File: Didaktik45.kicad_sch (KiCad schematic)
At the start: 110 parts, among them J1 Conn_01x04_MountingPin, SW1 SW_Push, SW10 SW_Push_45deg, SW11 SW_Push_45deg, SW12 SW_Push_45deg, SW13 SW_Push_45deg, SW14 SW_Push_45deg, SW15 SW_Push_45deg, SW16 SW_Push_45deg, SW17 SW_Push_45deg, SW18 SW_Push_45deg, SW19 SW_Push_45deg, SW2 SW_Push_45deg, SW20 SW_Push_45deg, SW21 SW_Push_45deg, SW22 SW_Push_45deg, SW23 SW_Push_45deg, SW24 SW_Push_45deg, SW25 SW_Push_45deg, SW26 SW_Push_45deg, SW27 SW_Push_45deg, SW28 SW_Push_45deg, SW29 SW_Push_45deg, SW3 SW_Push_45deg, SW30 SW_Push_45deg, SW31 SW_Push_45deg, SW32 SW_Push_45deg, SW33 SW_Push_45deg, SW34 SW_Push_45deg, SW35 SW_Push_45deg, SW36 SW_Push_45deg, SW37 SW_Push_45deg, SW38 SW_Push_45deg, SW39 SW_Push_45deg, SW4 SW_Push_45deg, SW40 SW_Push_45deg, SW41 SW_Push_45deg, SW42 SW_Push_45deg, SW43 SW_Push_45deg, SW44 SW_Push_45deg, SW45 SW_Push_45deg, SW46 SW_Push_45deg, SW5 SW_Push_45deg, SW6 SW_Push_45deg, SW7 SW_Push_45deg, SW8 SW_Push_45deg, SW9 SW_Push_45deg, U1 ATmega32U4-M, Y1 Crystal_GND24_Small

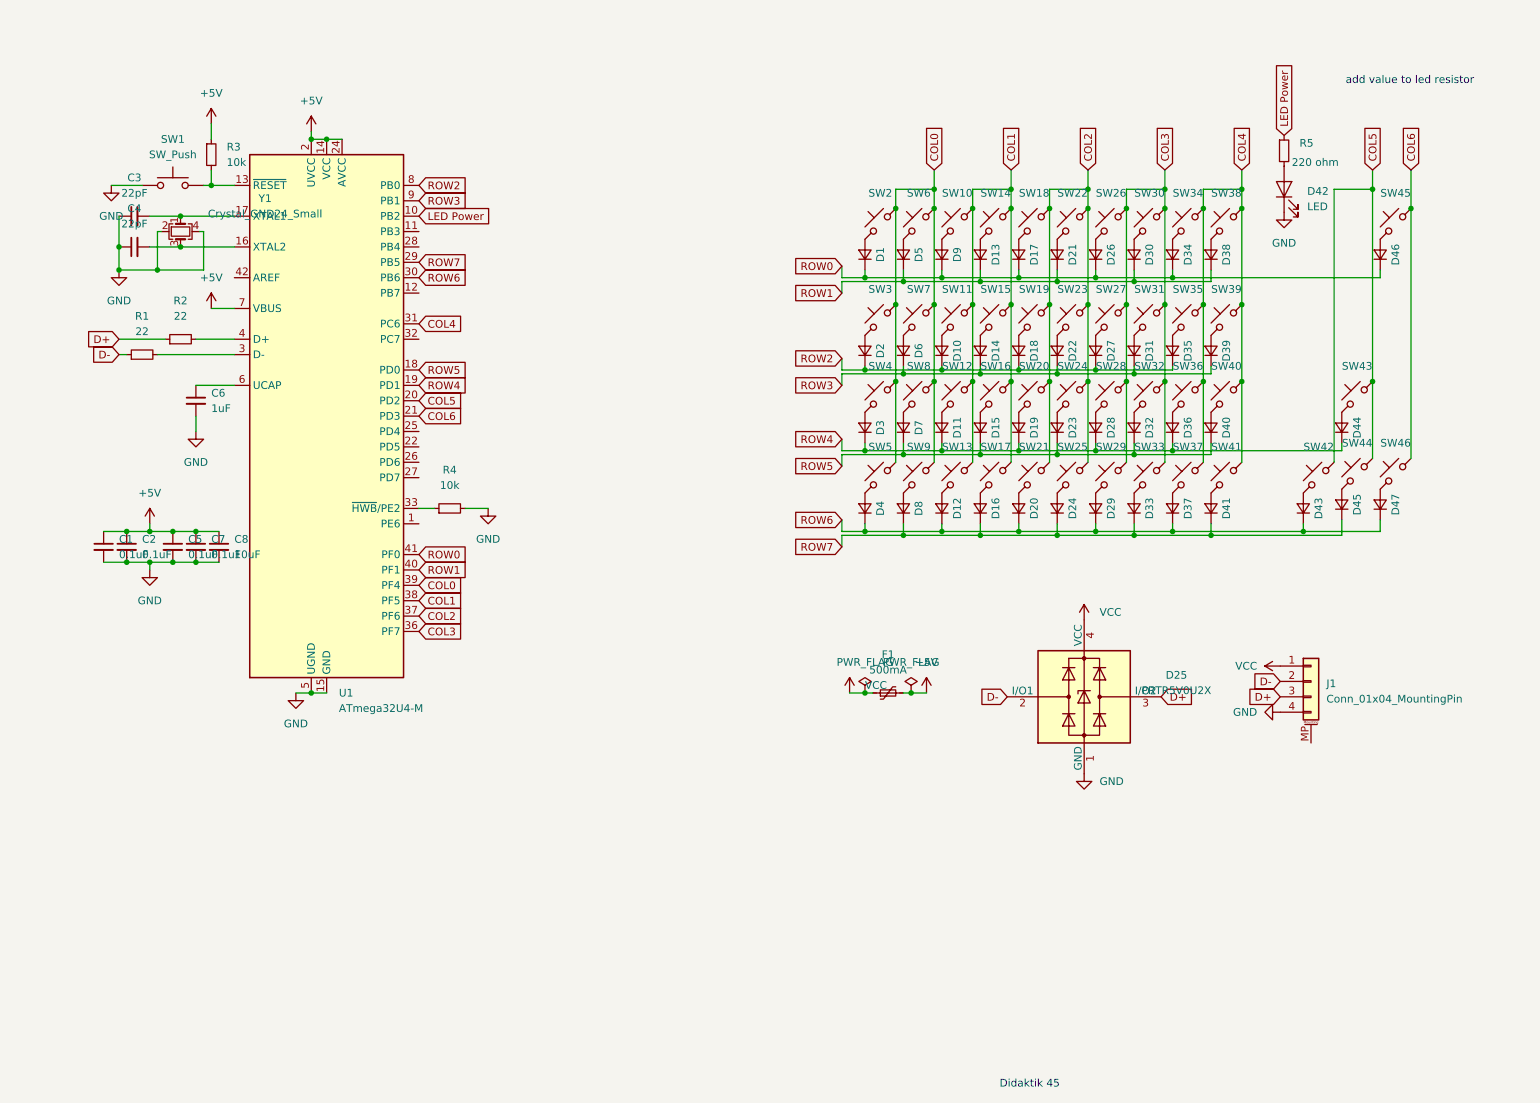
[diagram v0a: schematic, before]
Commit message: added ISP to 40, added ISP schematics to 45
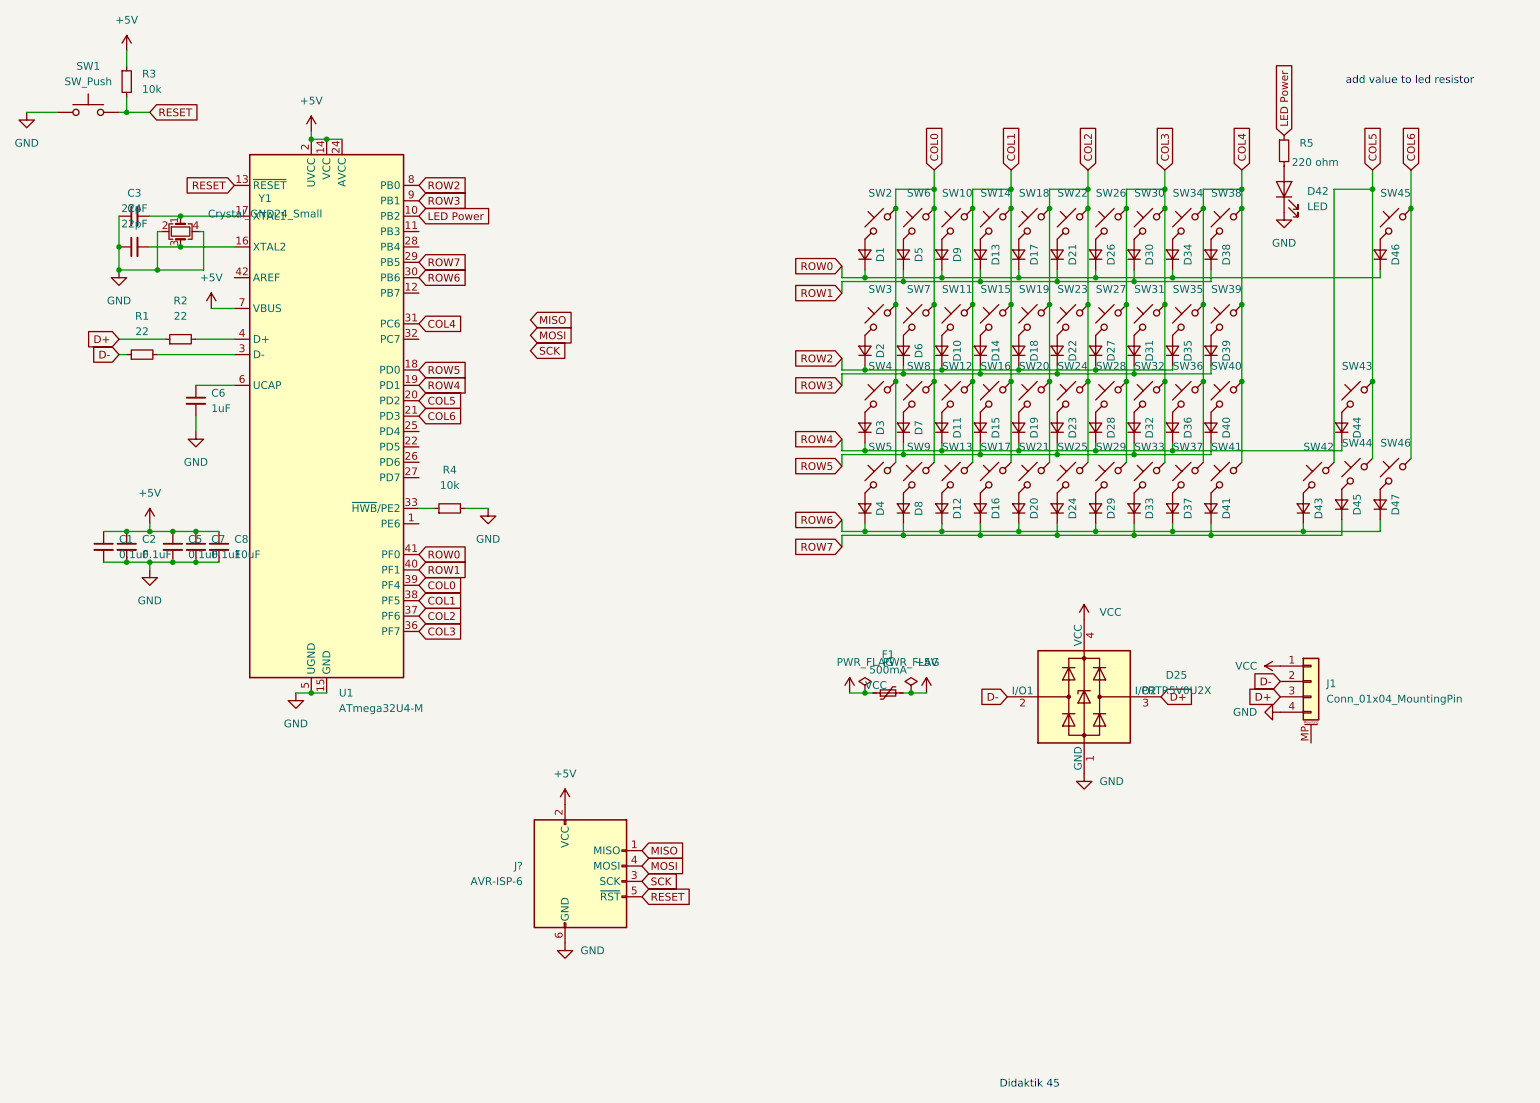
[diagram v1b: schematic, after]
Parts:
- added J?: AVR-ISP-6, random-keyboard-parts:Reset_Pretty-Mask, symbol Connector:AVR-ISP-6
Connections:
- net +5V: now also J?.2 (VCC)
- net GND: now also J?.6 (GND)
- net RESET: now reaches R3.2, SW1.2, U1.13 (~{RESET})
- net RESET: now also J?.5 (~{RST})
- new net MISO: J?.1 (MISO)
- new net MOSI: J?.4 (MOSI)
- new net SCK: J?.3 (SCK)
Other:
- moved on the sheet: R3, SW1

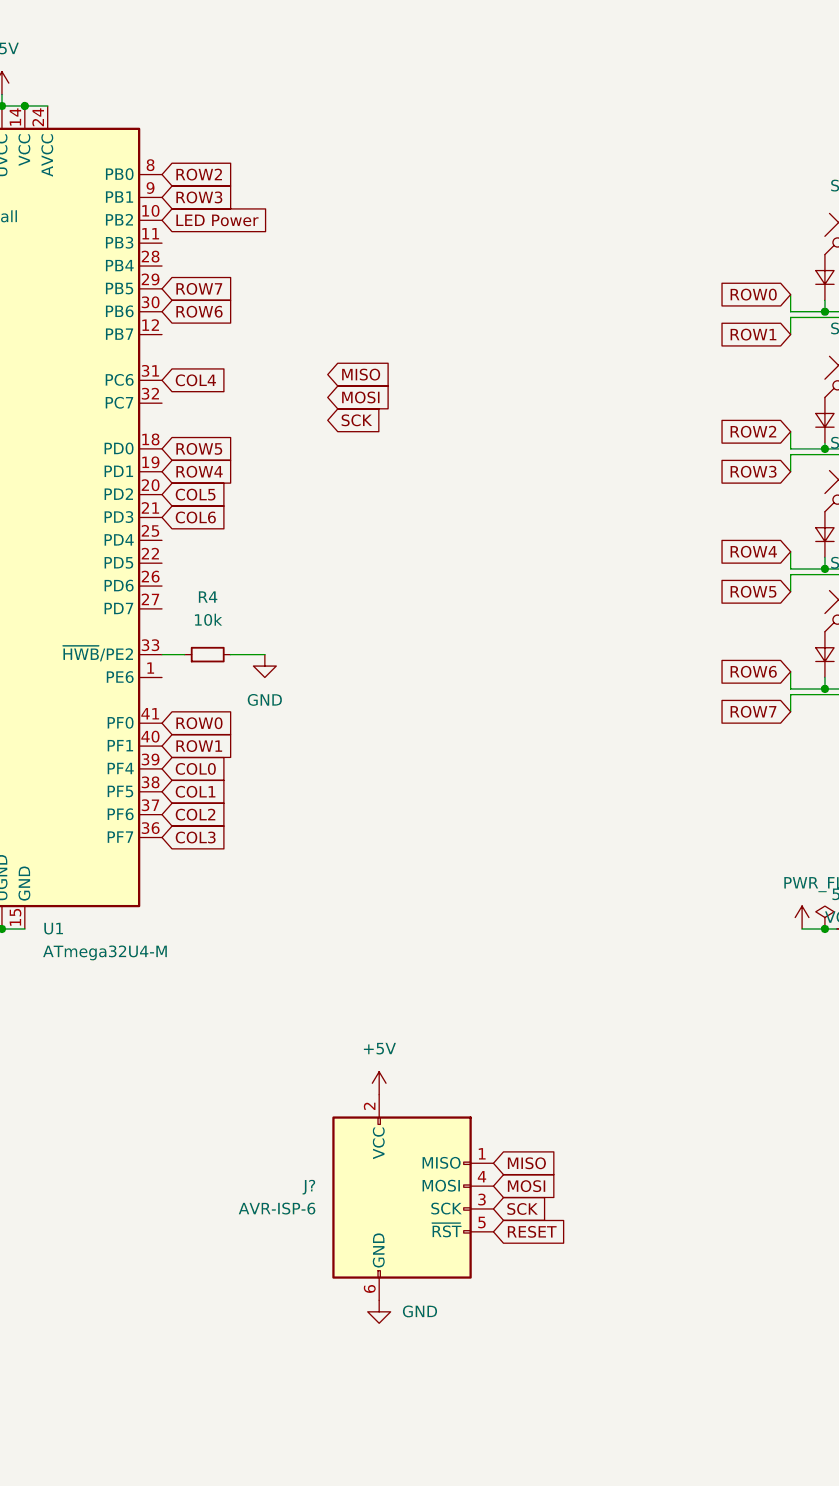
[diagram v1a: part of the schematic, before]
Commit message: added multi layout proto
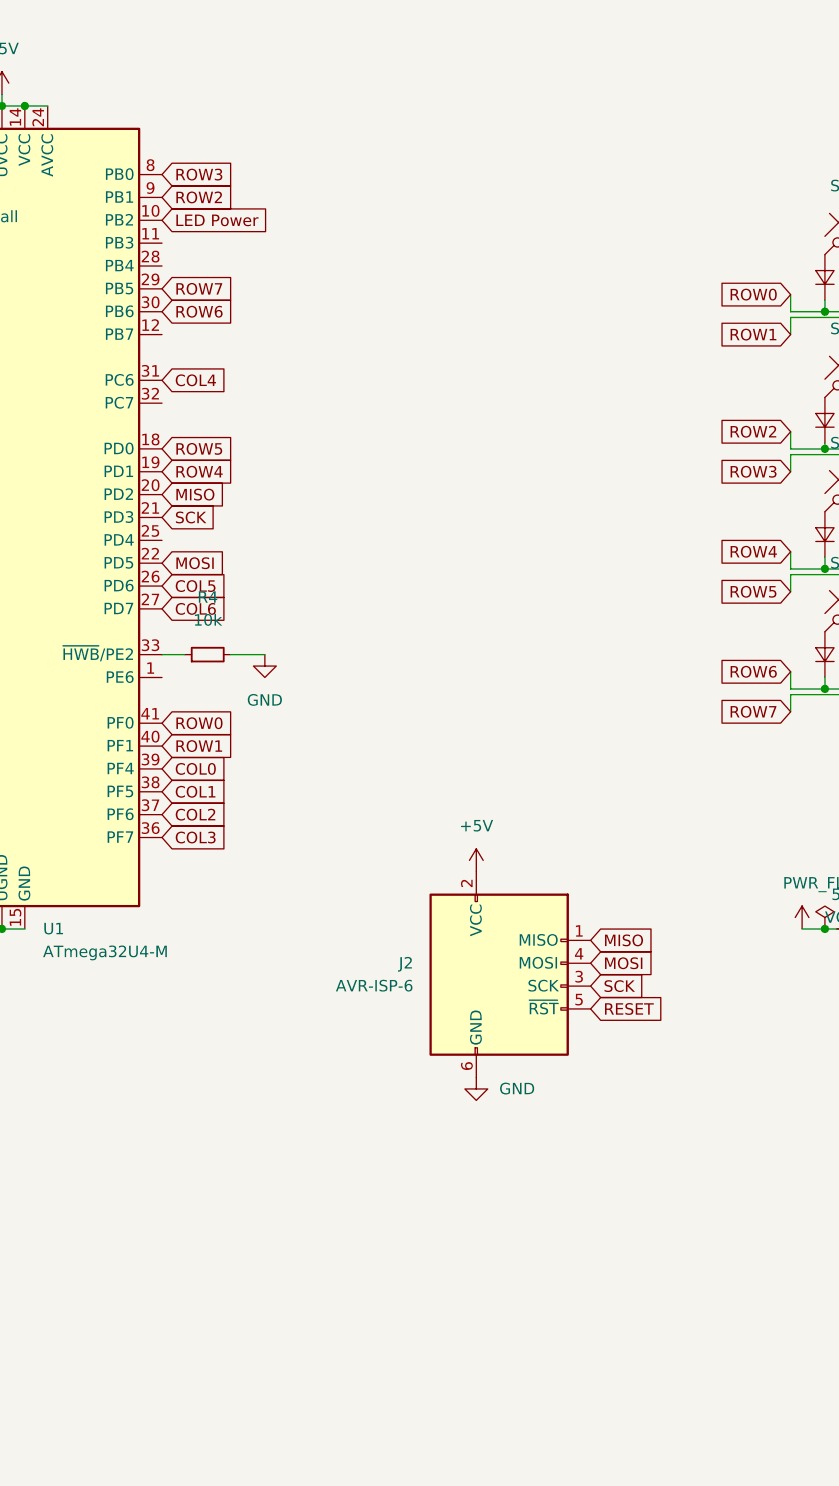
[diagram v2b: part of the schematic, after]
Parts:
- gave numbers to parts that had none: 1
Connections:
- net COL5: now also U1.26 (PD6); no longer U1.20 (PD2)
- net COL6: now also U1.27 (PD7); no longer U1.21 (PD3)
- net MISO: now also U1.20 (PD2)
- net MOSI: now also U1.22 (PD5)
- net ROW2: now also U1.9 (PB1); no longer U1.8 (PB0)
- net ROW3: now also U1.8 (PB0); no longer U1.9 (PB1)
- net SCK: now also U1.21 (PD3)
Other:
- moved on the sheet: J2
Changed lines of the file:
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@@
     )
   )
-  (global_label "COL6" (shape input) (at 92.075 79.375 0) (fields_autoplaced)
+  (global_label "COL6" (shape input) (at 92.075 89.535 0) (fields_autoplaced)
     (effects (font (size 1.27 1.27)) (justify left))
-    (property "Intersheet References" "${INTERSHEET_REFS}" (id 0) (at 99.3262 79.2956 0)
-      (effects (font (size 1.27 1.27)) (justify left) hide)
-    )
-  )
-  (global_label "ROW2" (shape input) (at 92.075 41.275 0) (fields_autoplaced)
+    (property "Intersheet References" "${INTERSHEET_REFS}" (id 0) (at 99.3262 89.4556 0)
+      (effects (font (size 1.27 1.27)) (justify left) hide)
+    )
+  )
+  (global_label "ROW2" (shape input) (at 92.075 43.815 0) (fields_autoplaced)
     (effects (font (size 1.27 1.27)) (justify left))
-    (property "Intersheet References" "${INTERSHEET_REFS}" (id 0) (at 99.7495 41.3544 0)
+    (property "Intersheet References" "${INTERSHEET_REFS}" (id 0) (at 99.7495 43.8944 0)
       (effects (font (size 1.27 1.27)) (justify left) hide)
     )
@@
     )
   )
-  (global_label "SCK" (shape input) (at 110.49 68.58 0) (fields_autoplaced)
+  (global_label "SCK" (shape input) (at 92.075 79.375 0) (fields_autoplaced)
     (effects (font (size 1.27 1.27)) (justify left))
-    (property "Intersheet References" "${INTERSHEET_REFS}" (id 0) (at 116.6526 68.5006 0)
+    (property "Intersheet References" "${INTERSHEET_REFS}" (id 0) (at 98.2376 79.2956 0)
       (effects (font (size 1.27 1.27)) (justify left) hide)
     )
@@
     )
   )
-  (global_label "MOSI" (shape input) (at 128.905 153.67 0) (fields_autoplaced)
+  (global_label "MOSI" (shape input) (at 139.7 128.905 0) (fields_autoplaced)
     (effects (font (size 1.27 1.27)) (justify left))
-    (property "Intersheet References" "${INTERSHEET_REFS}" (id 0) (at 135.9143 153.5906 0)
-      (effects (font (size 1.27 1.27)) (justify left) hide)
-    )
-  )
-  (global_label "COL5" (shape input) (at 92.075 76.835 0) (fields_autoplaced)
+    (property "Intersheet References" "${INTERSHEET_REFS}" (id 0) (at 146.7093 128.8256 0)
+      (effects (font (size 1.27 1.27)) (justify left) hide)
+    )
+  )
+  (global_label "COL5" (shape input) (at 92.075 86.995 0) (fields_autoplaced)
     (effects (font (size 1.27 1.27)) (justify left))
-    (property "Intersheet References" "${INTERSHEET_REFS}" (id 0) (at 99.3262 76.7556 0)
+    (property "Intersheet References" "${INTERSHEET_REFS}" (id 0) (at 99.3262 86.9156 0)
       (effects (font (size 1.27 1.27)) (justify left) hide)
     )
@@
     )
   )
-  (global_label "SCK" (shape input) (at 128.905 156.21 0) (fields_autoplaced)
+  (global_label "SCK" (shape input) (at 139.7 131.445 0) (fields_autoplaced)
     (effects (font (size 1.27 1.27)) (justify left))
-    (property "Intersheet References" "${INTERSHEET_REFS}" (id 0) (at 135.0676 156.1306 0)
+    (property "Intersheet References" "${INTERSHEET_REFS}" (id 0) (at 145.8626 131.3656 0)
       (effects (font (size 1.27 1.27)) (justify left) hide)
     )
@@
     )
   )
-  (global_label "ROW3" (shape input) (at 92.075 43.815 0) (fields_autoplaced)
+  (global_label "ROW3" (shape input) (at 92.075 41.275 0) (fields_autoplaced)
     (effects (font (size 1.27 1.27)) (justify left))
-    (property "Intersheet References" "${INTERSHEET_REFS}" (id 0) (at 99.7495 43.8944 0)
+    (property "Intersheet References" "${INTERSHEET_REFS}" (id 0) (at 99.7495 41.3544 0)
       (effects (font (size 1.27 1.27)) (justify left) hide)
     )
@@
     )
   )
-  (global_label "MOSI" (shape input) (at 110.49 66.04 0) (fields_autoplaced)
+  (global_label "MOSI" (shape input) (at 92.075 84.455 0) (fields_autoplaced)
     (effects (font (size 1.27 1.27)) (justify left))
-    (property "Intersheet References" "${INTERSHEET_REFS}" (id 0) (at 117.4993 65.9606 0)
+    (property "Intersheet References" "${INTERSHEET_REFS}" (id 0) (at 99.0843 84.3756 0)
       (effects (font (size 1.27 1.27)) (justify left) hide)
     )
@@
     )
   )
-  (global_label "MISO" (shape input) (at 110.49 63.5 0) (fields_autoplaced)
+  (global_label "MISO" (shape input) (at 92.075 76.835 0) (fields_autoplaced)
     (effects (font (size 1.27 1.27)) (justify left))
-    (property "Intersheet References" "${INTERSHEET_REFS}" (id 0) (at 117.4993 63.4206 0)
+    (property "Intersheet References" "${INTERSHEET_REFS}" (id 0) (at 99.0843 76.7556 0)
       (effects (font (size 1.27 1.27)) (justify left) hide)
     )
@@
     )
   )
-  (global_label "MISO" (shape input) (at 128.905 151.13 0) (fields_autoplaced)
+  (global_label "MISO" (shape input) (at 139.7 126.365 0) (fields_autoplaced)
     (effects (font (size 1.27 1.27)) (justify left))
-    (property "Intersheet References" "${INTERSHEET_REFS}" (id 0) (at 135.9143 151.0506 0)
-      (effects (font (size 1.27 1.27)) (justify left) hide)
-    )
-  )
-  (global_label "RESET" (shape input) (at 128.905 158.75 0) (fields_autoplaced)
+    (property "Intersheet References" "${INTERSHEET_REFS}" (id 0) (at 146.7093 126.2856 0)
+      (effects (font (size 1.27 1.27)) (justify left) hide)
+    )
+  )
+  (global_label "RESET" (shape input) (at 139.7 133.985 0) (fields_autoplaced)
     (effects (font (size 1.27 1.27)) (justify left))
-    (property "Intersheet References" "${INTERSHEET_REFS}" (id 0) (at 137.0633 158.6706 0)
+    (property "Intersheet References" "${INTERSHEET_REFS}" (id 0) (at 147.8583 133.9056 0)
       (effects (font (size 1.27 1.27)) (justify left) hide)
     )
@@
     (pin "2")
   )
-  (symbol (lib_id "power:+5V") (at 116.205 143.51 0) (unit 1)
-    (in_bom yes) (on_board yes) (fields_autoplaced)
-    (property "Reference" "#PWR?" (id 0) (at 116.205 147.32 0)
-      (effects (font (size 1.27 1.27)) hide)
-    )
-    (property "Value" "+5V" (id 1) (at 116.205 138.43 0))
-    (property "Footprint" "" (id 2) (at 116.205 143.51 0)
-      (effects (font (size 1.27 1.27)) hide)
-    )
-    (property "Datasheet" "" (id 3) (at 116.205 143.51 0)
+  (symbol (lib_id "power:+5V") (at 127 118.745 0) (unit 1)
+    (in_bom yes) (on_board yes) (fields_autoplaced)
+    (property "Reference" "#PWR0118" (id 0) (at 127 122.555 0)
+      (effects (font (size 1.27 1.27)) hide)
+    )
+    (property "Value" "+5V" (id 1) (at 127 113.665 0))
+    (property "Footprint" "" (id 2) (at 127 118.745 0)
+      (effects (font (size 1.27 1.27)) hide)
+    )
+    (property "Datasheet" "" (id 3) (at 127 118.745 0)
       (effects (font (size 1.27 1.27)) hide)
     )
@@
     (pin "2")
   )
-  (symbol (lib_id "power:GND") (at 116.205 166.37 0) (unit 1)
-    (in_bom yes) (on_board yes) (fields_autoplaced)
-    (property "Reference" "#PWR?" (id 0) (at 116.205 172.72 0)
-      (effects (font (size 1.27 1.27)) hide)
-    )
-    (property "Value" "GND" (id 1) (at 118.745 167.6399 0)
+  (symbol (lib_id "power:GND") (at 127 141.605 0) (unit 1)
+    (in_bom yes) (on_board yes) (fields_autoplaced)
+    (property "Reference" "#PWR0119" (id 0) (at 127 147.955 0)
+      (effects (font (size 1.27 1.27)) hide)
+    )
+    (property "Value" "GND" (id 1) (at 129.54 142.8749 0)
       (effects (font (size 1.27 1.27)) (justify left))
     )
-    (property "Footprint" "" (id 2) (at 116.205 166.37 0)
-      (effects (font (size 1.27 1.27)) hide)
-    )
-    (property "Datasheet" "" (id 3) (at 116.205 166.37 0)
+    (property "Footprint" "" (id 2) (at 127 141.605 0)
+      (effects (font (size 1.27 1.27)) hide)
+    )
+    (property "Datasheet" "" (id 3) (at 127 141.605 0)
       (effects (font (size 1.27 1.27)) hide)
     )
@@
     (pin "2")
   )
-  (symbol (lib_id "Connector:AVR-ISP-6") (at 118.745 156.21 0) (unit 1)
-    (in_bom yes) (on_board yes) (fields_autoplaced)
-    (property "Reference" "J?" (id 0) (at 109.22 153.6699 0)
+  (symbol (lib_id "Connector:AVR-ISP-6") (at 129.54 131.445 0) (unit 1)
+    (in_bom yes) (on_board yes) (fields_autoplaced)
+    (property "Reference" "J2" (id 0) (at 120.015 128.9049 0)
       (effects (font (size 1.27 1.27)) (justify right))
     )
-    (property "Value" "AVR-ISP-6" (id 1) (at 109.22 156.2099 0)
+    (property "Value" "AVR-ISP-6" (id 1) (at 120.015 131.4449 0)
       (effects (font (size 1.27 1.27)) (justify right))
     )
-    (property "Footprint" "random-keyboard-parts:Reset_Pretty-Mask" (id 2) (at 112.395 154.94 90)
-      (effects (font (size 1.27 1.27)) hide)
-    )
-    (property "Datasheet" " ~" (id 3) (at 86.36 170.18 0)
+    (property "Footprint" "random-keyboard-parts:Reset_Pretty-Mask" (id 2) (at 123.19 130.175 90)
+      (effects (font (size 1.27 1.27)) hide)
+    )
+    (property "Datasheet" " ~" (id 3) (at 97.155 145.415 0)
       (effects (font (size 1.27 1.27)) hide)
     )
@@
     )
     (path "/15c40bdf-c0d3-4f02-8968-e6da0c7b274d"
-      (reference "#PWR?") (unit 1) (value "+5V") (footprint "")
+      (reference "#PWR0118") (unit 1) (value "+5V") (footprint "")
     )
     (path "/35178b7e-6ef9-4124-a7ef-34cc28c325e2"
-      (reference "#PWR?") (unit 1) (value "GND") (footprint "")
+      (reference "#PWR0119") (unit 1) (value "GND") (footprint "")
     )
     (path "/4288a19a-13d9-4091-890e-2cc91277147e"
@@
     )
     (path "/4a6141cd-7d1f-4735-9bf3-d60ee4ed4433"
-      (reference "J?") (unit 1) (value "AVR-ISP-6") (footprint "random-keyboard-parts:Reset_Pretty-Mask")
+      (reference "J2") (unit 1) (value "AVR-ISP-6") (footprint "random-keyboard-parts:Reset_Pretty-Mask")
     )
     (path "/1b233532-9656-4e4e-a0b7-8260db2f2d5f"
